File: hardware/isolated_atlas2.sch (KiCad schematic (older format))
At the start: 17 parts, among them J401 CONN_01X02, P4 ATLAS_PH_PROBE, U401 ADM3260, U402 ATLAS_PH

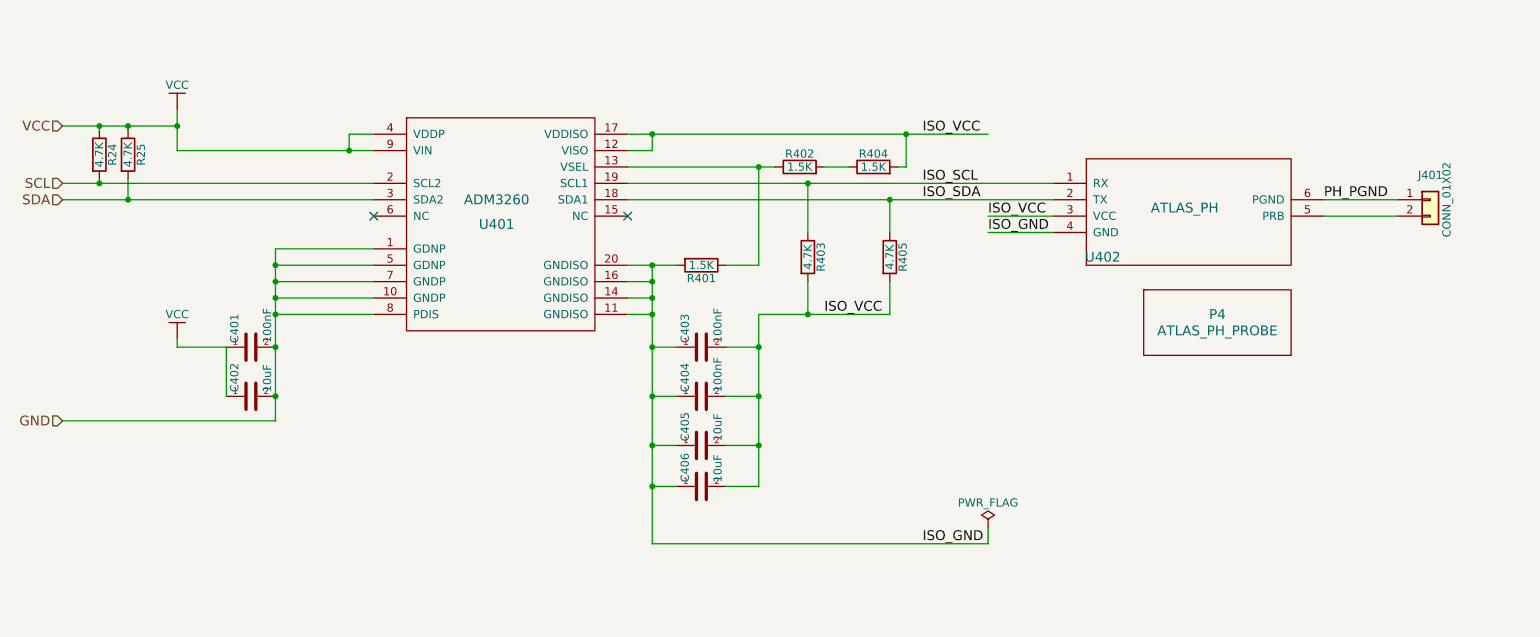
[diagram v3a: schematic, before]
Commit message: Generated panelized version of v0.11, including gerbers
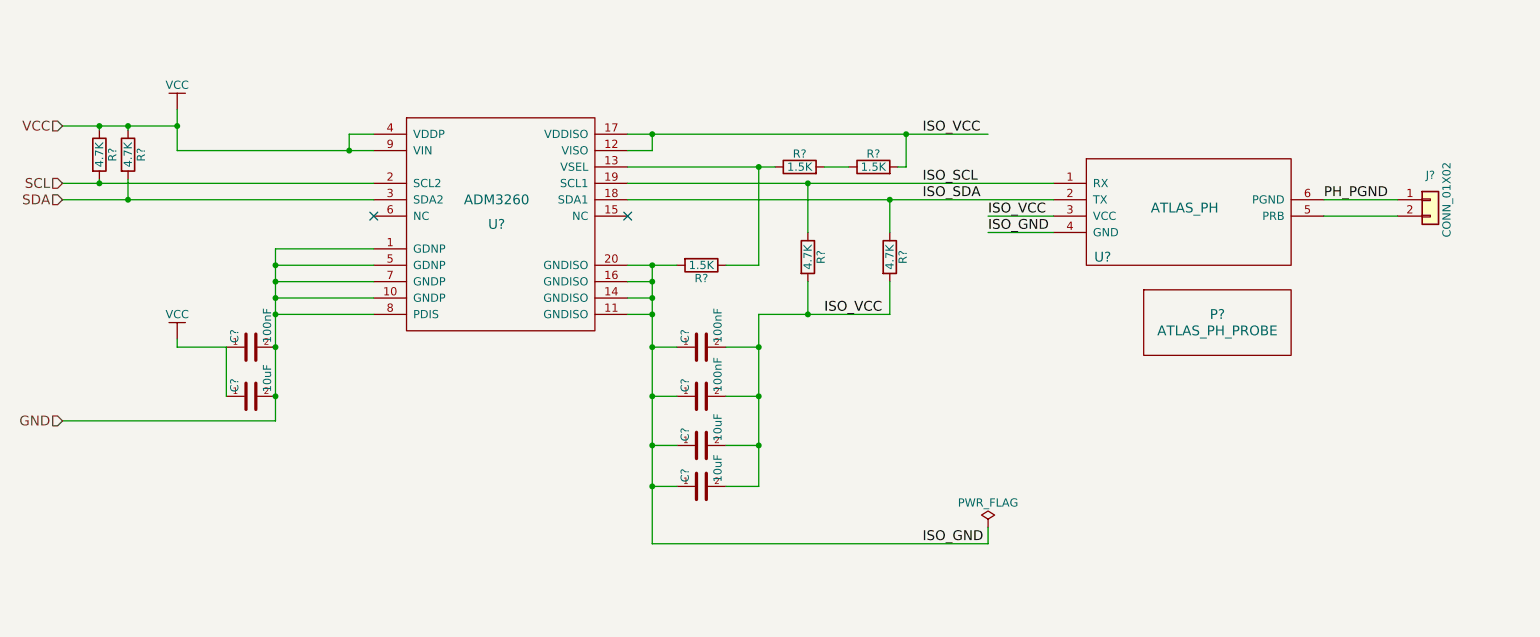
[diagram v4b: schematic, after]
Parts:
- renumbered C403 to C?, C404 to C?, C405 to C?, C406 to C?, C401 to C?, C402 to C?, J401 to J?, P4 to P?, R403 to R?, R401 to R?, R402 to R?, R404 to R?, R405 to R?, R24 to R?, R25 to R?, U401 to U?, U402 to U?
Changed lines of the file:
@@
 $EndDescr
 $Comp
-L fk-atlas-rescue:ADM3260-conservify U401
+L fk-atlas-rescue:ADM3260-conservify U?
 U 1 1 594C2CF1
 P 4400 2900
-F 0 "U401" H 4400 2750 60  0000 C CNN
+F 0 "U?" H 4400 2750 60  0000 C CNN
 F 1 "ADM3260" H 4400 2900 60  0000 C CNN
 F 2 "conservify:SSOP20-53" H 4400 2900 60  0001 C CNN
@@
 $EndComp
 $Comp
-L fk-atlas-rescue:CAPACITOR_CERAMIC-conservify C403
+L fk-atlas-rescue:CAPACITOR_CERAMIC-conservify C?
 U 1 1 594C2CF4
 P 5650 3800
-F 0 "C403" H 5675 3900 50  0000 L CNN
+F 0 "C?" H 5675 3900 50  0000 L CNN
 F 1 "100nF" H 5675 3700 50  0000 L CNN
 F 2 "conservify:CAP-0603" H 5688 3650 50  0001 C CNN
@@
 $EndComp
 $Comp
-L fk-atlas-rescue:CAPACITOR_CERAMIC-conservify C404
+L fk-atlas-rescue:CAPACITOR_CERAMIC-conservify C?
 U 1 1 594C2CF8
 P 5650 4100
-F 0 "C404" H 5675 4200 50  0000 L CNN
+F 0 "C?" H 5675 4200 50  0000 L CNN
 F 1 "100nF" H 5675 4000 50  0000 L CNN
 F 2 "conservify:CAP-0603" H 5688 3950 50  0001 C CNN
@@
 $EndComp
 $Comp
-L fk-atlas-rescue:CAPACITOR_CERAMIC-conservify C405
+L fk-atlas-rescue:CAPACITOR_CERAMIC-conservify C?
 U 1 1 594C2CFB
 P 5650 4400
-F 0 "C405" H 5675 4500 50  0000 L CNN
+F 0 "C?" H 5675 4500 50  0000 L CNN
 F 1 "10uF" H 5675 4300 50  0000 L CNN
 F 2 "conservify:CAP-0603" H 5688 4250 50  0001 C CNN
@@
 $EndComp
 $Comp
-L fk-atlas-rescue:CAPACITOR_CERAMIC-conservify C406
+L fk-atlas-rescue:CAPACITOR_CERAMIC-conservify C?
 U 1 1 594C2CFF
 P 5650 4650
-F 0 "C406" H 5675 4750 50  0000 L CNN
+F 0 "C?" H 5675 4750 50  0000 L CNN
 F 1 "10uF" H 5675 4550 50  0000 L CNN
 F 2 "conservify:CAP-0603" H 5688 4500 50  0001 C CNN
@@
 $EndComp
 $Comp
-L fk-atlas-rescue:CAPACITOR_CERAMIC-conservify C401
+L fk-atlas-rescue:CAPACITOR_CERAMIC-conservify C?
 U 1 1 594C2D03
 P 2900 3800
-F 0 "C401" H 2925 3900 50  0000 L CNN
+F 0 "C?" H 2925 3900 50  0000 L CNN
 F 1 "100nF" H 2925 3700 50  0000 L CNN
 F 2 "conservify:CAP-0603" H 2938 3650 50  0001 C CNN
@@
 $EndComp
 $Comp
-L fk-atlas-rescue:CAPACITOR_CERAMIC-conservify C402
+L fk-atlas-rescue:CAPACITOR_CERAMIC-conservify C?
 U 1 1 594C2D07
 P 2900 4100
-F 0 "C402" H 2925 4200 50  0000 L CNN
+F 0 "C?" H 2925 4200 50  0000 L CNN
 F 1 "10uF" H 2925 4000 50  0000 L CNN
 F 2 "conservify:CAP-0603" H 2938 3950 50  0001 C CNN
@@
 $EndComp
 $Comp
-L fk-atlas-rescue:R-conservify R401
+L fk-atlas-rescue:R-conservify R?
 U 1 1 594C2D0B
 P 5650 3300
-F 0 "R401" V 5730 3300 50  0000 C CNN
+F 0 "R?" V 5730 3300 50  0000 C CNN
 F 1 "1.5K" V 5650 3300 50  0000 C CNN
 F 2 "conservify:RES-0603" V 5580 3300 50  0001 C CNN
@@
 $EndComp
 $Comp
-L fk-atlas-rescue:R-conservify R402
+L fk-atlas-rescue:R-conservify R?
 U 1 1 594C2D10
 P 6250 2700
-F 0 "R402" V 6330 2700 50  0000 C CNN
+F 0 "R?" V 6330 2700 50  0000 C CNN
 F 1 "1.5K" V 6250 2700 50  0000 C CNN
 F 2 "conservify:RES-0603" V 6180 2700 50  0001 C CNN
@@
 $EndComp
 $Comp
-L fk-atlas-rescue:R-conservify R404
+L fk-atlas-rescue:R-conservify R?
 U 1 1 594C2D14
 P 6700 2700
-F 0 "R404" V 6780 2700 50  0000 C CNN
+F 0 "R?" V 6780 2700 50  0000 C CNN
 F 1 "1.5K" V 6700 2700 50  0000 C CNN
 F 2 "conservify:RES-0603" V 6630 2700 50  0001 C CNN
@@
 $EndComp
 $Comp
-L fk-atlas-rescue:R-conservify R403
+L fk-atlas-rescue:R-conservify R?
 U 1 1 5948E450
 P 6300 3250
-F 0 "R403" V 6380 3250 50  0000 C CNN
+F 0 "R?" V 6380 3250 50  0000 C CNN
 F 1 "4.7K" V 6300 3250 50  0000 C CNN
 F 2 "conservify:RES-0603" V 6230 3250 50  0001 C CNN
@@
 $EndComp
 $Comp
-L fk-atlas-rescue:R-conservify R405
+L fk-atlas-rescue:R-conservify R?
 U 1 1 594C2D1B
 P 6800 3250
-F 0 "R405" V 6880 3250 50  0000 C CNN
+F 0 "R?" V 6880 3250 50  0000 C CNN
 F 1 "4.7K" V 6800 3250 50  0000 C CNN
 F 2 "conservify:RES-0603" V 6730 3250 50  0001 C CNN
@@
 $EndComp
 $Comp
-L fk-atlas-rescue:VCC-conservify #PWR061
+L fk-atlas-rescue:VCC-conservify #PWR?
 U 1 1 594C2D24
 P 2450 3750
-F 0 "#PWR061" H 2450 3600 50  0001 C CNN
+F 0 "#PWR?" H 2450 3600 50  0001 C CNN
 F 1 "VCC" H 2450 3900 50  0000 C CNN
 F 2 "" H 2450 3750 50  0001 C CNN
@@
 $EndComp
 $Comp
-L fk-atlas-rescue:VCC-conservify #PWR062
+L fk-atlas-rescue:VCC-conservify #PWR?
 U 1 1 594C2D2A
 P 2450 2350
-F 0 "#PWR062" H 2450 2200 50  0001 C CNN
+F 0 "#PWR?" H 2450 2200 50  0001 C CNN
 F 1 "VCC" H 2450 2500 50  0000 C CNN
 F 2 "" H 2450 2350 50  0001 C CNN
@@
 $EndComp
 $Comp
-L fk-atlas-rescue:ATLAS_SENSOR-conservify U402
+L fk-atlas-rescue:ATLAS_SENSOR-conservify U?
 U 1 1 594C2D35
 P 8550 2900
-F 0 "U402" H 8100 2550 60  0000 C CNN
+F 0 "U?" H 8100 2550 60  0000 C CNN
 F 1 "ATLAS_PH" H 8600 2850 60  0000 C CNN
 F 2 "conservify:ATLAS_SENSOR_BOARD_COMBO" H 8550 2900 60  0001 C CNN
@@
 $EndComp
 $Comp
-L fk-atlas-rescue:CONN_01x02-conservify J401
+L fk-atlas-rescue:CONN_01x02-conservify J?
 U 1 1 59A1BC7D
 P 10100 2900
-F 0 "J401" H 10100 3050 50  0000 C CNN
+F 0 "J?" H 10100 3050 50  0000 C CNN
 F 1 "CONN_01X02" V 10200 2900 50  0000 C CNN
 F 2 "conservify:BNC" H 10100 2900 50  0001 C CNN
@@
 $EndComp
 $Comp
-L fk-atlas-rescue:ATLAS_WATER_PROBE-conservify P4
+L fk-atlas-rescue:ATLAS_WATER_PROBE-conservify P?
 U 1 1 59D2A29B
 P 8800 3600
-F 0 "P4" H 8800 3600 60  0000 C CNN
+F 0 "P?" H 8800 3600 60  0000 C CNN
 F 1 "ATLAS_PH_PROBE" H 8800 3500 60  0000 C CNN
 F 2 "conservify:Dummy_Empty" H 8800 3600 60  0001 C CNN
@@
 $EndComp
 $Comp
-L fk-atlas-rescue:PWR_FLAG-conservify #FLG0107
+L fk-atlas-rescue:PWR_FLAG-conservify #FLG?
 U 1 1 5BCC2A39
 P 7400 4900
-F 0 "#FLG0107" H 7400 4975 50  0001 C CNN
+F 0 "#FLG?" H 7400 4975 50  0001 C CNN
 F 1 "PWR_FLAG" H 7400 5050 50  0000 C CNN
 F 2 "" H 7400 4900 50  0001 C CNN
@@
 NoConn ~ 5200 3000
 $Comp
-L fk-atlas-rescue:R-conservify R24
+L fk-atlas-rescue:R-conservify R?
 U 1 1 5C7FF88D
 P 1975 2625
-F 0 "R24" V 2055 2625 50  0000 C CNN
+F 0 "R?" V 2055 2625 50  0000 C CNN
 F 1 "4.7K" V 1975 2625 50  0000 C CNN
 F 2 "conservify:RES-0603" V 1905 2625 50  0001 C CNN
@@
 	1975 2800 3650 2800
 $Comp
-L fk-atlas-rescue:R-conservify R25
+L fk-atlas-rescue:R-conservify R?
 U 1 1 5C803402
 P 2150 2625
-F 0 "R25" V 2230 2625 50  0000 C CNN
+F 0 "R?" V 2230 2625 50  0000 C CNN
 F 1 "4.7K" V 2150 2625 50  0000 C CNN
 F 2 "conservify:RES-0603" V 2080 2625 50  0001 C CNN
